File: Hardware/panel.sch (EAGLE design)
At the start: 18 parts, among them X1 B16B-PHDSS, X2 52746-20

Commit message: разъем под шлейф,вывод для штатного питания прибора. Сделал цепи комутации кнопок на транзисторе.
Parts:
- added C2: 0.33uF, rcl:CPOL-EUCT3216
- added C3: 0.1uF, rcl:CPOL-EUCT3216
- added PAD1: (no value), wirepad:1,6/0,8
- added Q1, Q2, Q3, Q4, Q5: BC817-40LT1SMD, transistor-npn:BC817-40LT1SMD
- added R1, R10, R11, R12, R4, R5, R6, R7, R8, R9: 4.7k, rcl:R-EU_R0805
- added U1: MC7805CDT, _hhn_78xx_79xx_NCV78xx_d2pak_dpak:MC7805CDT
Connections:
- new net +24V: C2.+, U1.VIN, X2-17.S, X2-18.S, X2-19.S, X2-20.S
- new net FF_SIG: R12.2, X2-9.S
- new net FN_SIG: R10.2, X2-8.S
- new net LASER_SIG: R8.2, X2-7.S
- new net N$1: Q1.B, R1.2, R4.1
- new net N$3: S3.0@A, S3.0@B
- new net N$4: Q2.B, R5.2, R6.1
- new net N$5: Q3.B, R7.2, R8.1
- new net N$6: Q4.B, R10.1, R9.2
- new net N$7: Q5.B, R11.2, R12.1
- new net PRW_SIG: R4.2, X2-5.S
- new net SET_SIG: R6.2, X2-6.S
- new net VOUT_SB: C3.+, PAD1.P, U1.VOUT
- net FFSW: now also Q5.C
- net FNSW: now also Q4.C
- net GND: now also C2.-, C3.-, Q1.E, Q2.E, Q3.E, Q4.E, Q5.E, R1.1, R11.1, R5.1, R7.1, R9.1, U1.GND, X2-1.S, X2-2.S, X2-3.S, X2-4.S; no longer S3.0@A, S3.0@B
- net LASERSW: now also Q3.C
- net PWR_SW: now also Q1.C
- net SETSW: now also Q2.C
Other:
- moved on the sheet: LED1, LED2, LED3, LED4, LED5, S1, S3, S4, S5, X1, X2-1, X2-10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

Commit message: переподключил индикаторы через транзисторы. это надо испытать
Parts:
- added Q10, Q11, Q12, Q6, Q7, Q8, Q9: BC807-16LT1SMD, transistor-pnp:BC807-16LT1SMD
- added Q13, Q14, Q15, Q16, Q17, Q18, Q19: BC817-40LT1SMD, transistor-npn:BC817-40LT1SMD
- added R13, R15, R16, R18, R19, R21, R22, R24, R25, R27, R28, R30, R31, R33, R34, R36, R38, R40, R42, R44, R46: 4.7k, rcl:R-EU_R0805
- added R14, R17, R20, R23, R26, R29, R32: 2.2k, rcl:R-EU_R0805
- added R35, R37, R39, R41, R43, R45, R47: 800, rcl:R-EU_R0805
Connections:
- new net ADJLED_SIG: LED2.A, Q9.C, X2-11.S
- new net DOWNLED_SIG: LED3.A, Q10.C, X2-12.S
- new net LVLLED_SIG: LED7.A, Q6.C, X2-16.S
- new net N$10: LED7.C, R14.2
- new net N$11: Q14.B, R36.1, R37.2
- new net N$12: Q7.B, R15.1, R18.1
- new net N$13: LED6.C, R17.2
- new net N$14: Q8.B, R19.1, R21.1
- new net N$15: LED1.C, R20.2
- new net N$16: Q9.B, R22.1, R24.1
- new net N$17: LED2.C, R23.2
- new net N$18: Q10.B, R25.1, R27.1
- new net N$19: LED3.C, R26.2
- new net N$20: Q11.B, R28.1, R30.1
- new net N$21: LED4.C, R29.2
- new net N$22: Q12.B, R31.1, R33.1
- new net N$23: LED5.C, R32.2
- new net N$24: Q13.B, R34.1, R35.2
- new net N$25: Q14.C, R15.2
- new net N$26: Q15.B, R38.1, R39.2
- new net N$27: Q15.C, R31.2
- new net N$28: Q16.B, R40.1, R41.2
- new net N$29: Q16.C, R28.2
- new net N$30: Q17.B, R42.1, R43.2
- new net N$31: Q17.C, R25.2
- new net N$32: Q18.B, R44.1, R45.2
- new net N$33: Q18.C, R22.2
- new net N$34: Q19.B, R46.1, R47.2
- new net N$35: Q19.C, R19.2
- new net N$8: Q6.B, R13.1, R16.1
- new net N$9: Q13.C, R13.2
- new net PWRLED_SIG: LED1.A, Q8.C, X2-10.S
- new net UPLED_SIG: LED6.A, Q7.C, X2-15.S
- new net XLED_SIG: LED4.A, Q11.C, X2-13.S
- new net YLED_SIG: LED5.A, Q12.C, X2-14.S
- net +24V: now also Q10.E, Q11.E, Q12.E, Q6.E, Q7.E, Q8.E, Q9.E, R16.2, R18.2, R21.2, R24.2, R27.2, R30.2, R33.2
- net +5V: now also R35.1, R37.1, R39.1, R41.1, R43.1, R45.1, R47.1; no longer LED1.A, LED2.A, LED3.A, LED4.A, LED5.A, LED6.A, LED7.A
- net ADJLED: now also Q18.E, R44.2; no longer LED2.C
- net DOWNLED: now also Q17.E, R42.2; no longer LED3.C
- net GND: now also R14.1, R17.1, R20.1, R23.1, R26.1, R29.1, R32.1
- net LVLED: now also Q13.E, R34.2; no longer LED7.C
- net PWRLED: now also Q19.E, R46.2; no longer LED1.C
- net UPLED: now also Q14.E, R36.2; no longer LED6.C
- net XLED: now also Q16.E, R40.2; no longer LED4.C
- net YLED: now also Q15.E, R38.2; no longer LED5.C
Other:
- moved on the sheet: C2, C3, LED1, LED2, LED3, LED4, LED5, LED6, LED7, PAD1, Q1, R1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

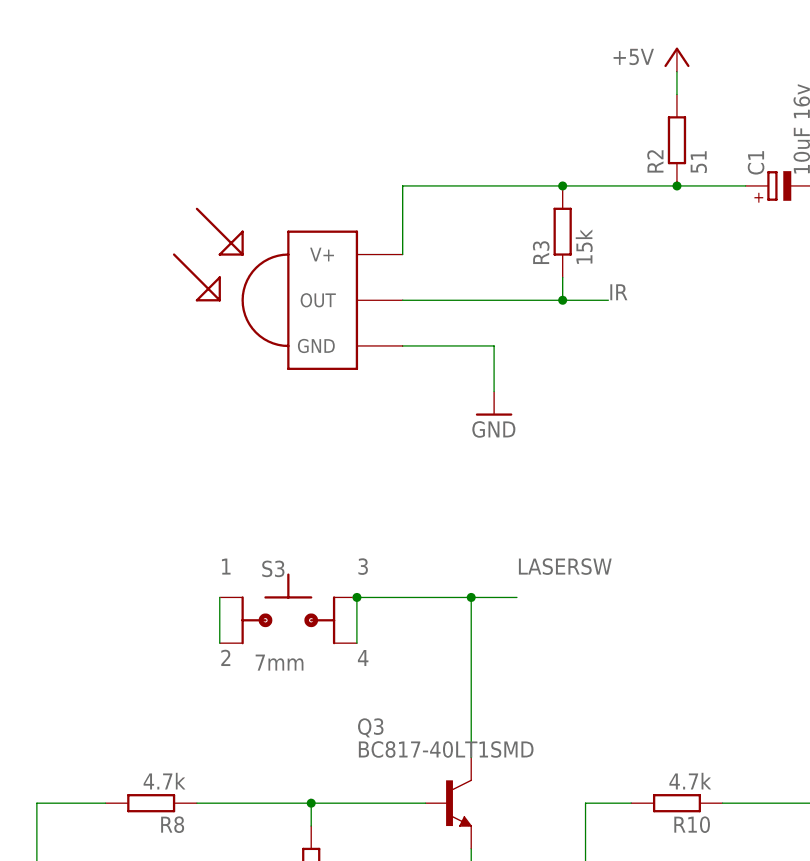
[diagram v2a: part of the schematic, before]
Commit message: сделал разводку управляющих и индикаторных цепей на транзисторах. еще не проверял работоспособность решений.
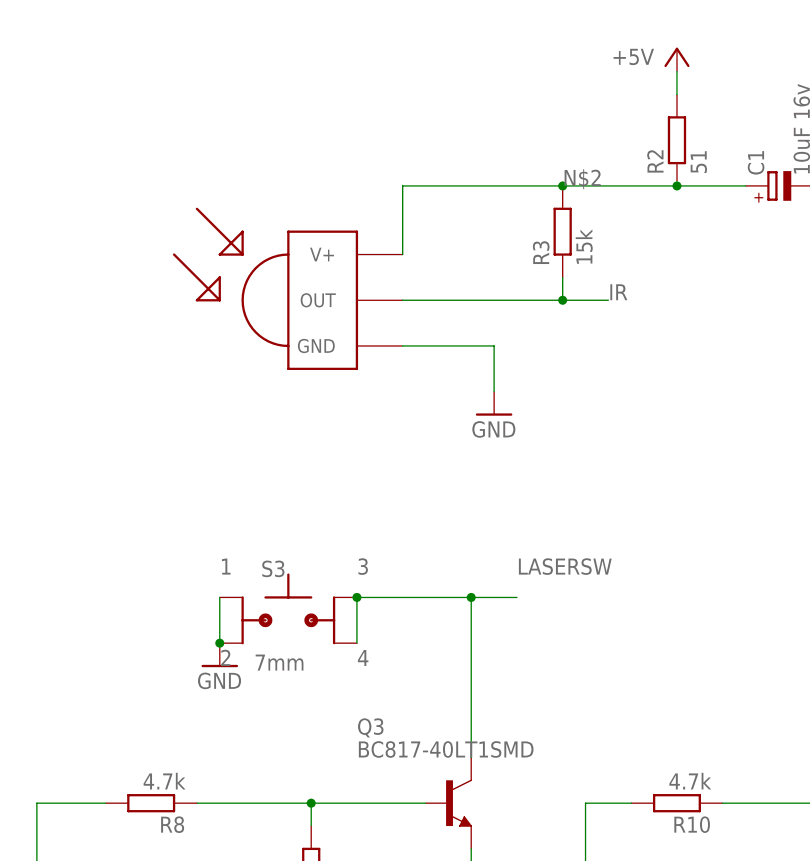
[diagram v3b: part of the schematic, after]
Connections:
- removed net N$3: S3.0@A, S3.0@B
- net GND: now also S3.0@A, S3.0@B
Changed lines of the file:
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@@
 </class>
 <class number="1" name="supply" width="0.254" drill="0">
-<clearance class="1" value="0.1778"/>
+<clearance class="1" value="0.127"/>
 </class>
 <class number="2" name="signal" width="0.254" drill="0">
 <clearance class="2" value="0.254"/>
+</class>
+<class number="3" name="thermal" width="0" drill="0">
 </class>
 </classes>
@@
 <part name="R46" library="rcl" library_urn="urn:adsk.eagle:library:334" deviceset="R-EU_" device="R0805" package3d_urn="urn:adsk.eagle:package:23553/2" value="4.7k"/>
 <part name="R47" library="rcl" library_urn="urn:adsk.eagle:library:334" deviceset="R-EU_" device="R0805" package3d_urn="urn:adsk.eagle:package:23553/2" value="800"/>
+<part name="GND22" library="supply1" library_urn="urn:adsk.eagle:library:371" deviceset="GND" device=""/>
 </parts>
 <sheets>
@@
 <attribute name="NAME" x="-128.0414" y="-54.61" size="1.778" layer="95" rot="R270"/>
 <attribute name="VALUE" x="-132.842" y="-54.61" size="1.778" layer="96" rot="R270"/>
+</instance>
+<instance part="GND22" gate="1" x="182.88" y="48.26" smashed="yes">
+<attribute name="VALUE" x="180.34" y="45.72" size="1.778" layer="96"/>
 </instance>
 </instances>
@@
 </segment>
 </net>
-<net name="GND" class="0">
+<net name="GND" class="1">
 <segment>
 <pinref part="S1" gate="G$1" pin="0@B"/>
@@
 <wire x1="365.76" y1="-86.36" x2="360.68" y2="-86.36" width="0.1524" layer="91"/>
 </segment>
+<segment>
+<pinref part="S3" gate="G$1" pin="0@B"/>
+<pinref part="S3" gate="G$1" pin="0@A"/>
+<wire x1="182.88" y1="55.88" x2="182.88" y2="50.8" width="0.1524" layer="91"/>
+<pinref part="GND22" gate="1" pin="GND"/>
+<junction x="182.88" y="50.8"/>
+</segment>
 </net>
 <net name="SETSW" class="2">
@@
 <pinref part="R3" gate="G$1" pin="2"/>
 <junction x="220.98" y="101.6"/>
+<label x="220.98" y="101.6" size="1.778" layer="95"/>
 </segment>
 </net>
@@
 </segment>
 </net>
-<net name="N$3" class="0">
-<segment>
-<pinref part="S3" gate="G$1" pin="0@B"/>
-<pinref part="S3" gate="G$1" pin="0@A"/>
-<wire x1="182.88" y1="55.88" x2="182.88" y2="50.8" width="0.1524" layer="91"/>
-</segment>
-</net>

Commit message: заменил библиотеку transistor-pnp на пользовательскую, скопировав исходную. Таким образом ушел глюк с исчезновением корпусов транзисторов bc807
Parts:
- Q10, Q11, Q12, Q6, Q7, Q8, Q9: device transistor-pnp:BC807-16LT1SMD -> transistor-pnp_user:BC807-16LT1SMD
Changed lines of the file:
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@@
 <part name="R11" library="rcl" library_urn="urn:adsk.eagle:library:334" deviceset="R-EU_" device="R0805" package3d_urn="urn:adsk.eagle:package:23553/2" value="4.7k"/>
 <part name="R12" library="rcl" library_urn="urn:adsk.eagle:library:334" deviceset="R-EU_" device="R0805" package3d_urn="urn:adsk.eagle:package:23553/2" value="4.7k"/>
-<part name="Q6" library="transistor-pnp" library_urn="urn:adsk.eagle:library:399" deviceset="BC807*" device="SMD" package3d_urn="urn:adsk.eagle:package:28748/2" technology="-16LT1" value="BC807-16LT1SMD"/>
+<part name="Q6" library="transistor-pnp_user" library_urn="urn:adsk.eagle:library:21050097" deviceset="BC807*" device="SMD" package3d_urn="urn:adsk.eagle:package:28748/2" technology="-16LT1" value="BC807-16LT1SMD"/>
 <part name="R13" library="rcl" library_urn="urn:adsk.eagle:library:334" deviceset="R-EU_" device="R0805" package3d_urn="urn:adsk.eagle:package:23553/2" value="4.7k"/>
 <part name="P+7" library="supply1" library_urn="urn:adsk.eagle:library:371" deviceset="+24V" device=""/>
@@
 <part name="R14" library="rcl" library_urn="urn:adsk.eagle:library:334" deviceset="R-EU_" device="R0805" package3d_urn="urn:adsk.eagle:package:23553/2" value="2.2k"/>
 <part name="R16" library="rcl" library_urn="urn:adsk.eagle:library:334" deviceset="R-EU_" device="R0805" package3d_urn="urn:adsk.eagle:package:23553/2" value="4.7k"/>
-<part name="Q7" library="transistor-pnp" library_urn="urn:adsk.eagle:library:399" deviceset="BC807*" device="SMD" package3d_urn="urn:adsk.eagle:package:28748/2" technology="-16LT1" value="BC807-16LT1SMD"/>
+<part name="Q7" library="transistor-pnp_user" library_urn="urn:adsk.eagle:library:21050097" deviceset="BC807*" device="SMD" package3d_urn="urn:adsk.eagle:package:28748/2" technology="-16LT1" value="BC807-16LT1SMD"/>
 <part name="R15" library="rcl" library_urn="urn:adsk.eagle:library:334" deviceset="R-EU_" device="R0805" package3d_urn="urn:adsk.eagle:package:23553/2" value="4.7k"/>
 <part name="P+8" library="supply1" library_urn="urn:adsk.eagle:library:371" deviceset="+24V" device=""/>
@@
 <part name="R17" library="rcl" library_urn="urn:adsk.eagle:library:334" deviceset="R-EU_" device="R0805" package3d_urn="urn:adsk.eagle:package:23553/2" value="2.2k"/>
 <part name="R18" library="rcl" library_urn="urn:adsk.eagle:library:334" deviceset="R-EU_" device="R0805" package3d_urn="urn:adsk.eagle:package:23553/2" value="4.7k"/>
-<part name="Q8" library="transistor-pnp" library_urn="urn:adsk.eagle:library:399" deviceset="BC807*" device="SMD" package3d_urn="urn:adsk.eagle:package:28748/2" technology="-16LT1" value="BC807-16LT1SMD"/>
+<part name="Q8" library="transistor-pnp_user" library_urn="urn:adsk.eagle:library:21050097" deviceset="BC807*" device="SMD" package3d_urn="urn:adsk.eagle:package:28748/2" technology="-16LT1" value="BC807-16LT1SMD"/>
 <part name="R19" library="rcl" library_urn="urn:adsk.eagle:library:334" deviceset="R-EU_" device="R0805" package3d_urn="urn:adsk.eagle:package:23553/2" value="4.7k"/>
 <part name="P+9" library="supply1" library_urn="urn:adsk.eagle:library:371" deviceset="+24V" device=""/>
@@
 <part name="R20" library="rcl" library_urn="urn:adsk.eagle:library:334" deviceset="R-EU_" device="R0805" package3d_urn="urn:adsk.eagle:package:23553/2" value="2.2k"/>
 <part name="R21" library="rcl" library_urn="urn:adsk.eagle:library:334" deviceset="R-EU_" device="R0805" package3d_urn="urn:adsk.eagle:package:23553/2" value="4.7k"/>
-<part name="Q9" library="transistor-pnp" library_urn="urn:adsk.eagle:library:399" deviceset="BC807*" device="SMD" package3d_urn="urn:adsk.eagle:package:28748/2" technology="-16LT1" value="BC807-16LT1SMD"/>
+<part name="Q9" library="transistor-pnp_user" library_urn="urn:adsk.eagle:library:21050097" deviceset="BC807*" device="SMD" package3d_urn="urn:adsk.eagle:package:28748/2" technology="-16LT1" value="BC807-16LT1SMD"/>
 <part name="R22" library="rcl" library_urn="urn:adsk.eagle:library:334" deviceset="R-EU_" device="R0805" package3d_urn="urn:adsk.eagle:package:23553/2" value="4.7k"/>
 <part name="P+10" library="supply1" library_urn="urn:adsk.eagle:library:371" deviceset="+24V" device=""/>
@@
 <part name="R23" library="rcl" library_urn="urn:adsk.eagle:library:334" deviceset="R-EU_" device="R0805" package3d_urn="urn:adsk.eagle:package:23553/2" value="2.2k"/>
 <part name="R24" library="rcl" library_urn="urn:adsk.eagle:library:334" deviceset="R-EU_" device="R0805" package3d_urn="urn:adsk.eagle:package:23553/2" value="4.7k"/>
-<part name="Q10" library="transistor-pnp" library_urn="urn:adsk.eagle:library:399" deviceset="BC807*" device="SMD" package3d_urn="urn:adsk.eagle:package:28748/2" technology="-16LT1" value="BC807-16LT1SMD"/>
+<part name="Q10" library="transistor-pnp_user" library_urn="urn:adsk.eagle:library:21050097" deviceset="BC807*" device="SMD" package3d_urn="urn:adsk.eagle:package:28748/2" technology="-16LT1" value="BC807-16LT1SMD"/>
 <part name="R25" library="rcl" library_urn="urn:adsk.eagle:library:334" deviceset="R-EU_" device="R0805" package3d_urn="urn:adsk.eagle:package:23553/2" value="4.7k"/>
 <part name="P+11" library="supply1" library_urn="urn:adsk.eagle:library:371" deviceset="+24V" device=""/>
@@
 <part name="R26" library="rcl" library_urn="urn:adsk.eagle:library:334" deviceset="R-EU_" device="R0805" package3d_urn="urn:adsk.eagle:package:23553/2" value="2.2k"/>
 <part name="R27" library="rcl" library_urn="urn:adsk.eagle:library:334" deviceset="R-EU_" device="R0805" package3d_urn="urn:adsk.eagle:package:23553/2" value="4.7k"/>
-<part name="Q11" library="transistor-pnp" library_urn="urn:adsk.eagle:library:399" deviceset="BC807*" device="SMD" package3d_urn="urn:adsk.eagle:package:28748/2" technology="-16LT1" value="BC807-16LT1SMD"/>
+<part name="Q11" library="transistor-pnp_user" library_urn="urn:adsk.eagle:library:21050097" deviceset="BC807*" device="SMD" package3d_urn="urn:adsk.eagle:package:28748/2" technology="-16LT1" value="BC807-16LT1SMD"/>
 <part name="R28" library="rcl" library_urn="urn:adsk.eagle:library:334" deviceset="R-EU_" device="R0805" package3d_urn="urn:adsk.eagle:package:23553/2" value="4.7k"/>
 <part name="P+12" library="supply1" library_urn="urn:adsk.eagle:library:371" deviceset="+24V" device=""/>
@@
 <part name="R29" library="rcl" library_urn="urn:adsk.eagle:library:334" deviceset="R-EU_" device="R0805" package3d_urn="urn:adsk.eagle:package:23553/2" value="2.2k"/>
 <part name="R30" library="rcl" library_urn="urn:adsk.eagle:library:334" deviceset="R-EU_" device="R0805" package3d_urn="urn:adsk.eagle:package:23553/2" value="4.7k"/>
-<part name="Q12" library="transistor-pnp" library_urn="urn:adsk.eagle:library:399" deviceset="BC807*" device="SMD" package3d_urn="urn:adsk.eagle:package:28748/2" technology="-16LT1" value="BC807-16LT1SMD"/>
+<part name="Q12" library="transistor-pnp_user" library_urn="urn:adsk.eagle:library:21050097" deviceset="BC807*" device="SMD" package3d_urn="urn:adsk.eagle:package:28748/2" technology="-16LT1" value="BC807-16LT1SMD"/>
 <part name="R31" library="rcl" library_urn="urn:adsk.eagle:library:334" deviceset="R-EU_" device="R0805" package3d_urn="urn:adsk.eagle:package:23553/2" value="4.7k"/>
 <part name="P+13" library="supply1" library_urn="urn:adsk.eagle:library:371" deviceset="+24V" device=""/>

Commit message: по результатам эксперимента с кнопками и индикаторами все нормально. оявилась идея добавить защитные резисторы на индикаторные выходы,чтобы не сгорал транзистор в случае кз на землю
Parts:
- added R48, R49, R50, R51, R52, R53, R54, R55, R56, R57, R58, R59, R60, R61: 150, rcl:R-EU_R2512
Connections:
- new net N$3: LED7.A, Q6.C, R48.1
- new net N$36: R48.2, R49.1
- new net N$37: LED6.A, Q7.C, R50.1
- new net N$38: R50.2, R51.1
- new net N$39: LED1.A, Q8.C, R52.1
- new net N$40: R52.2, R53.1
- new net N$41: LED2.A, Q9.C, R54.1
- new net N$42: R54.2, R55.1
- new net N$43: LED3.A, Q10.C, R56.1
- new net N$44: R56.2, R57.1
- new net N$45: LED4.A, Q11.C, R58.1
- new net N$46: R58.2, R59.1
- new net N$47: LED5.A, Q12.C, R60.1
- new net N$48: R60.2, R61.1
- net ADJLED_SIG: now also R55.2; no longer LED2.A, Q9.C
- net DOWNLED_SIG: now also R57.2; no longer LED3.A, Q10.C
- net LVLLED_SIG: now also R49.2; no longer LED7.A, Q6.C
- net PWRLED_SIG: now also R53.2; no longer LED1.A, Q8.C
- net UPLED_SIG: now also R51.2; no longer LED6.A, Q7.C
- net XLED_SIG: now also R59.2; no longer LED4.A, Q11.C
- net YLED_SIG: now also R61.2; no longer LED5.A, Q12.C
